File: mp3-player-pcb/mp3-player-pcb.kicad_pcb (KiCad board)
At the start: 2 copper layers, 68.8 x 99.2 mm, 39 parts, among them SW1 RotaryEncoder_Switch, SW2 Volume Up, SW3 Volume Down, U1 XIAO-ESP32-S3-Plus-SMD, U2 AO3407A, U3 MAX17048G+T10, U4 MAX98357A, U5 CR2013-MI2120

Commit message: feat: finished routing the pcb
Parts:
- moved SW1 3.68 mm to (112.8, 103.8)
- renumbered D- to TP1, D+ to TP2
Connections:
- U1 pad 1: unconnected-(U1-D0-Pad1) -> ScreenDataCommand
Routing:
- net Bat-: track 0.00 -> 295.6 mm, vias 0 -> 8
- net ScreenCS: track 0.00 -> 157.6 mm, vias 0 -> 2
- net 3v3_PERIPH: track 0.00 -> 151.6 mm, vias 0 -> 2
- net ScreenDataCommand: track 0.00 -> 110.1 mm, vias 0 -> 3
- net VolumeUpSW: track 0.00 -> 97.3 mm, vias 0 -> 3
- net Net-(JP8-B): track 0.00 -> 93.9 mm, vias 0 -> 3
- net Net-(JP9-B): track 0.00 -> 93.2 mm, vias 0 -> 3
- net ScreenReset: track 0.00 -> 91.1 mm, vias 0 -> 7
- net SD_CS: track 0.00 -> 89.1 mm
- net ScreenMOSI: track 0.00 -> 88.5 mm, vias 0 -> 4
- net ScreenMISO: track 0.00 -> 85.6 mm, vias 0 -> 6
- net Net-(JP7-B): track 0.00 -> 85.0 mm, vias 0 -> 3
- net ScreenCLK: track 0.00 -> 82.2 mm, vias 0 -> 4
- net VolumeDownSW: track 0.00 -> 73.7 mm, vias 0 -> 3
- net +3V3: track 0.00 -> 56.8 mm, vias 0 -> 4
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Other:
- board text added: "Speaker Gain Selector"
- board text added: "Yes the buttons & resistors are supposed to be here idc if it is in the courtyard of the screen The pins after soldering will be trimmed as low as possible so it WILL fit"

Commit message: feat: made case cad
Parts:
- added ?: , , F.Cu at (151.0, 134.4)
- added ?: , , F.Cu at (90.0, 134.6)
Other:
- outline, holes or cut-outs redrawn
- board text added: "+ -"
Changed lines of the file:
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@@
 		(embedded_fonts no)
 	)
+	(footprint ""
+		(layer "F.Cu")
+		(at 150.975 134.4)
+		(property "Reference" ""
+			(at 0 0 0)
+			(layer "F.SilkS")
+			(effects
+				(font
+					(size 1.27 1.27)
+				)
+			)
+		)
+		(property "Value" ""
+			(at 0 0 0)
+			(layer "F.Fab")
+			(effects
+				(font
+					(size 1.27 1.27)
+				)
+			)
+		)
+		(property "Datasheet" ""
+			(at 0 0 0)
+			(layer "F.Fab")
+			(hide yes)
+			(effects
+				(font
+					(size 1.27 1.27)
+				)
+			)
+		)
+		(property "Description" ""
+			(at 0 0 0)
+			(layer "F.Fab")
+			(hide yes)
+			(effects
+				(font
+					(size 1.27 1.27)
+				)
+			)
+		)
+		(duplicate_pad_numbers_are_jumpers no)
+		(pad "" thru_hole circle
+			(at 0 0)
+			(size 4 4)
+			(drill 2.7)
+			(layers "*.Cu" "*.Mask")
+			(remove_unused_layers no)
+		)
+		(embedded_fonts no)
+	)
 	(footprint "Resistor_THT:R_Axial_DIN0204_L3.6mm_D1.6mm_P5.08mm_Horizontal"
 		(layer "F.Cu")
@@
 		(embedded_fonts no)
 	)
+	(footprint ""
+		(layer "F.Cu")
+		(at 89.975 134.6)
+		(property "Reference" ""
+			(at 0 0 0)
+			(layer "F.SilkS")
+			(effects
+				(font
+					(size 1.27 1.27)
+				)
+			)
+		)
+		(property "Value" ""
+			(at 0 0 0)
+			(layer "F.Fab")
+			(effects
+				(font
+					(size 1.27 1.27)
+				)
+			)
+		)
+		(property "Datasheet" ""
+			(at 0 0 0)
+			(layer "F.Fab")
+			(hide yes)
+			(effects
+				(font
+					(size 1.27 1.27)
+				)
+			)
+		)
+		(property "Description" ""
+			(at 0 0 0)
+			(layer "F.Fab")
+			(hide yes)
+			(effects
+				(font
+					(size 1.27 1.27)
+				)
+			)
+		)
+		(duplicate_pad_numbers_are_jumpers no)
+		(pad "" thru_hole circle
+			(at 0 0)
+			(size 4 4)
+			(drill 2.7)
+			(layers "*.Cu" "*.Mask")
+			(remove_unused_layers no)
+		)
+		(embedded_fonts no)
+	)
 	(footprint "TestPoint:TestPoint_Pad_D1.5mm"
 		(layer "F.Cu")
@@
 	)
 	(gr_rect
-		(start 87.65 121.875)
-		(end 93.1 133.425)
+		(start 87.65 121.175)
+		(end 93.1 131.9)
 		(stroke
 			(width 0.05)
@@
 		(layer "Edge.Cuts")
 	)
-	(gr_text "Speaker Wire Hole"
-		(at 87.675 135.475 0)
+	(gr_text "+\n\n-"
+		(at 86.25 113.525 0)
 		(layer "F.SilkS")
 		(effects
@@
 		)
 	)
+	(gr_text "Speaker Wire Hole"
+		(at 92.35 135.25 0)
+		(layer "F.SilkS")
+		(effects
+			(font
+				(size 1 1)
+				(thickness 0.15)
+			)
+			(justify left bottom)
+		)
+	)
 	(gr_text "Speaker Gain Selector"
 		(at 96.175 98.875 0)
@@
 		(layer "F.SilkS")
 		(effects
+			(font
+				(size 1 1)
+				(thickness 0.15)
+			)
+			(justify left bottom)
+		)
+	)
+	(gr_text "+\n\n-"
+		(at 137.25 116.025 0)
+		(layer "F.SilkS")
+		(effects

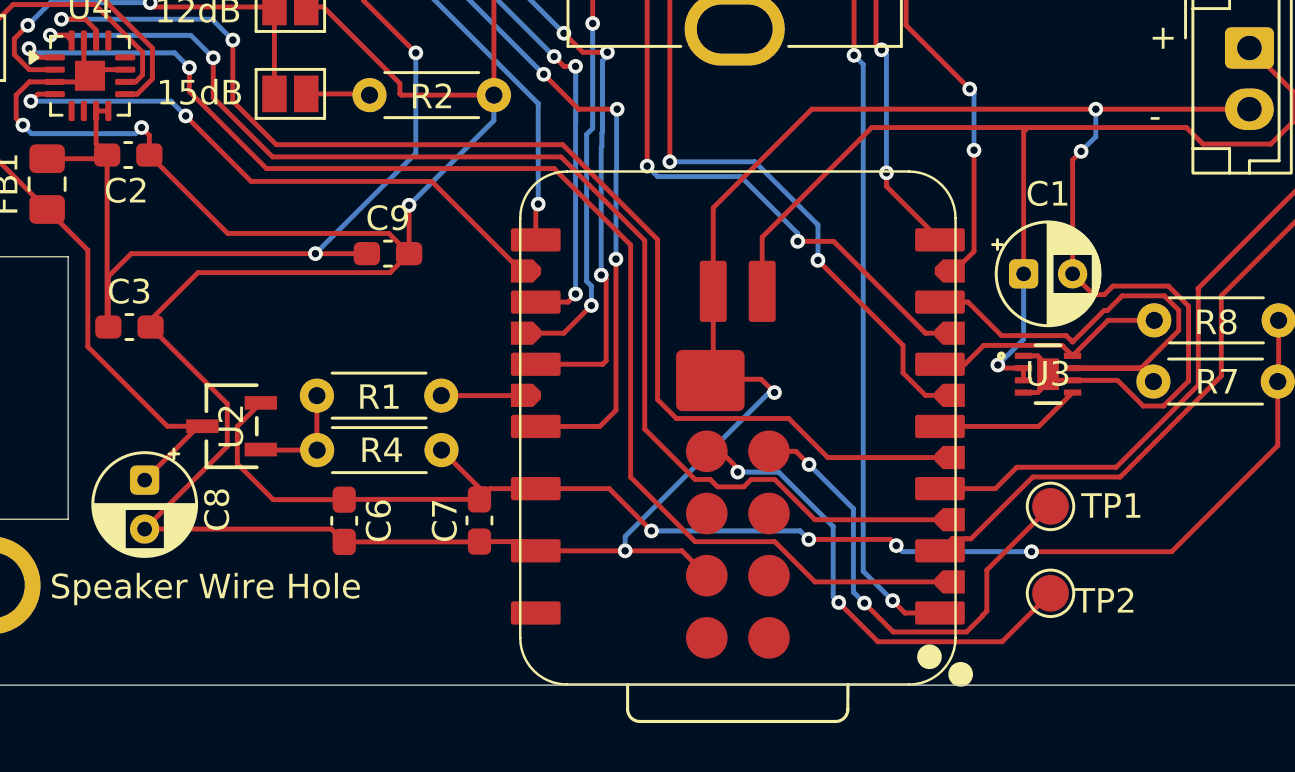
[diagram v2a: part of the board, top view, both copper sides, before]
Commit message: bom and other parts added
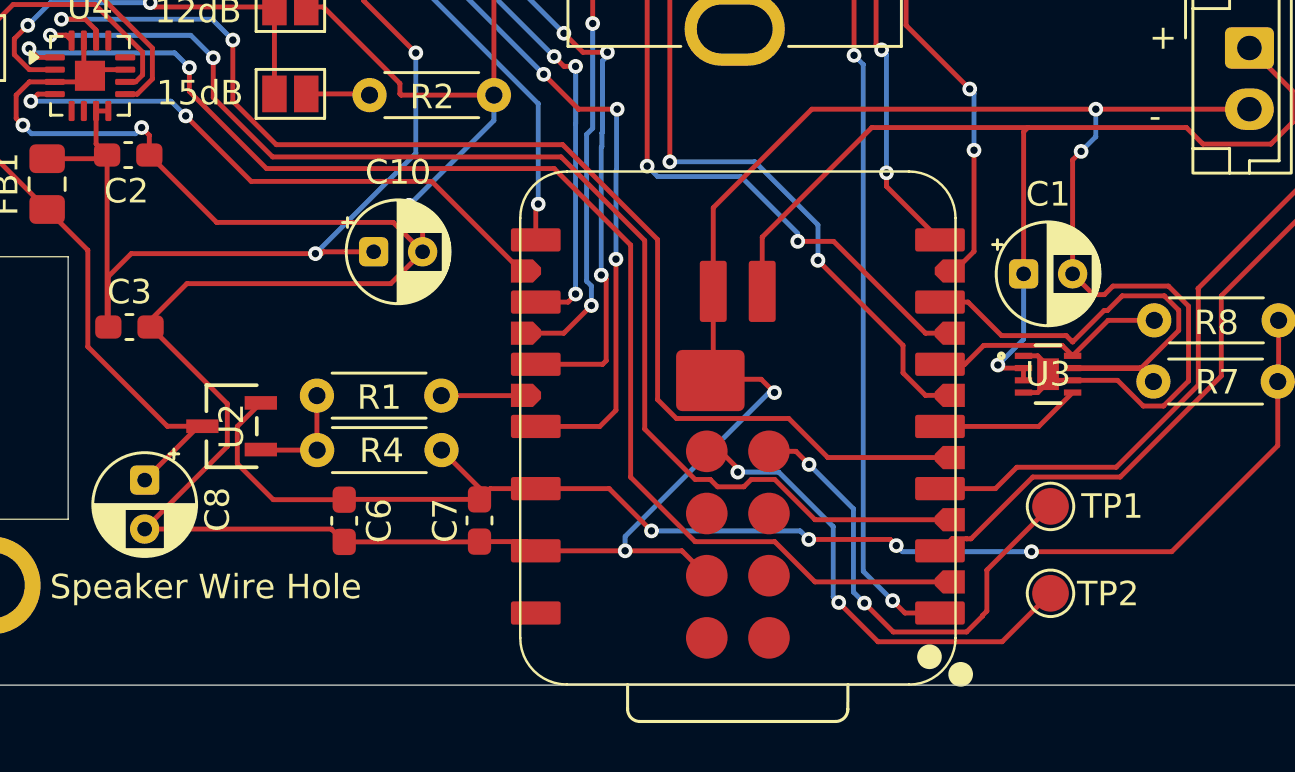
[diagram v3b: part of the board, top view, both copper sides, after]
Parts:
- removed C9: 100uF, Capacitor_SMD:C_0603_1608Metric_Pad1.08x0.95mm_HandSolder
- added C10: 100uF, Capacitor_THT:CP_Radial_D4.0mm_P2.00mm, F.Cu at (105.6, 121.0)
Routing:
- net Bat-: track 295.6 -> 296.9 mm
